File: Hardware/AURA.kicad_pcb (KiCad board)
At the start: 2 copper layers, 126.9 x 80.6 mm, 13 parts, among them SW1 EC11E18244AU, SW2 SW_Push, SW3 SW_Push, SW4 SW_Push, SW5 SW_Push, SW6 SW_Push, SW7 SW_Push, U1 ER_OLEDM0.91_1x-I2C

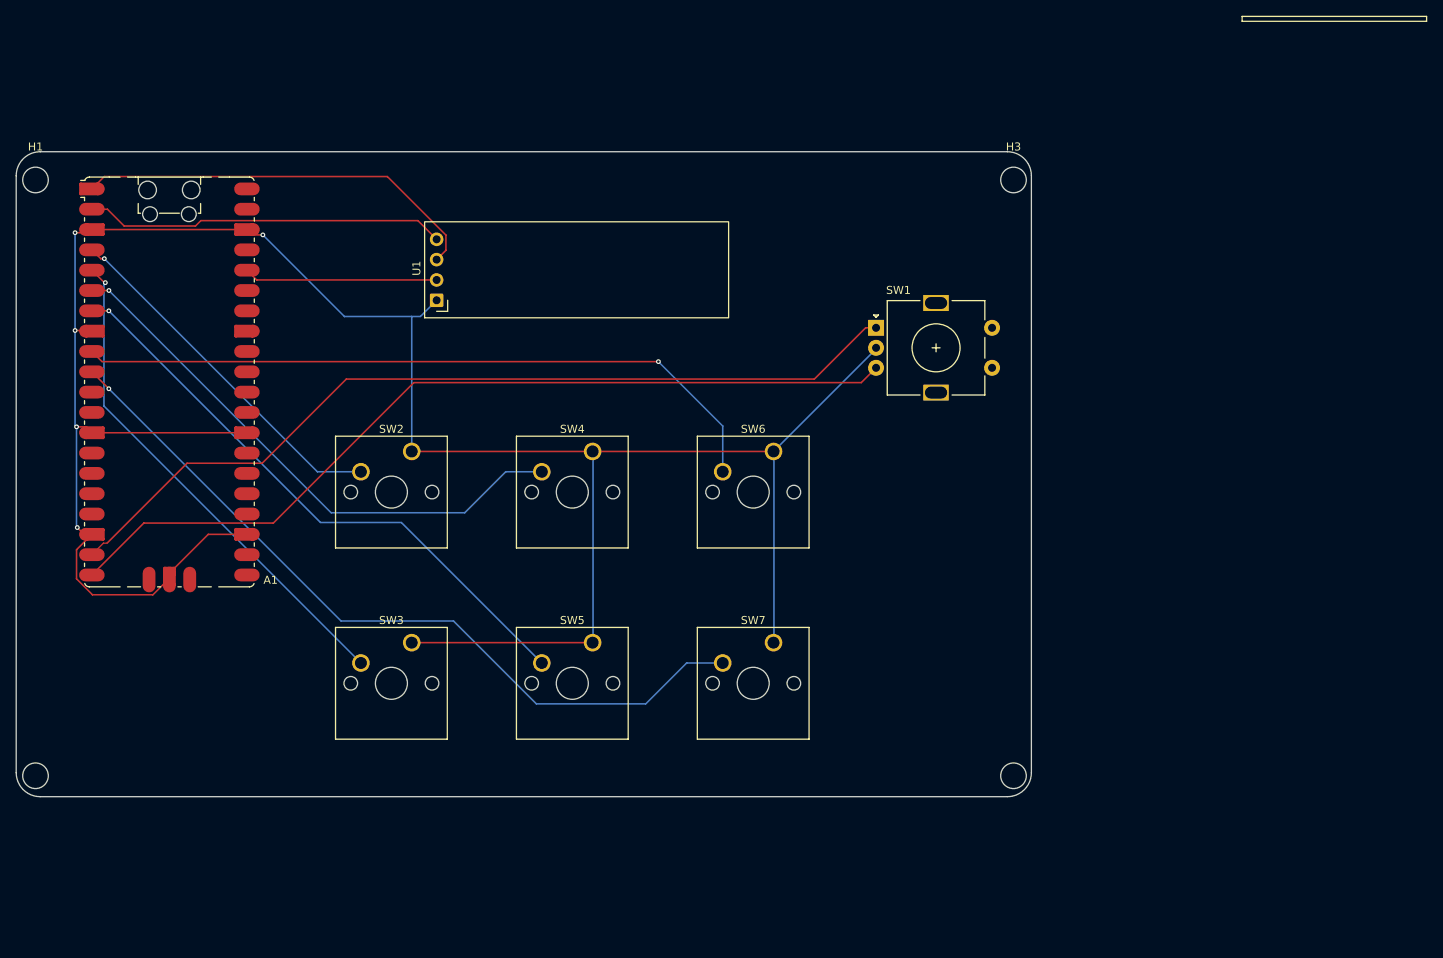
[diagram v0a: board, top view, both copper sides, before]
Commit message: AURA V2
Re-wrote the full readme. added the new .step file of the PCB, and added all the required file for the enclosure.
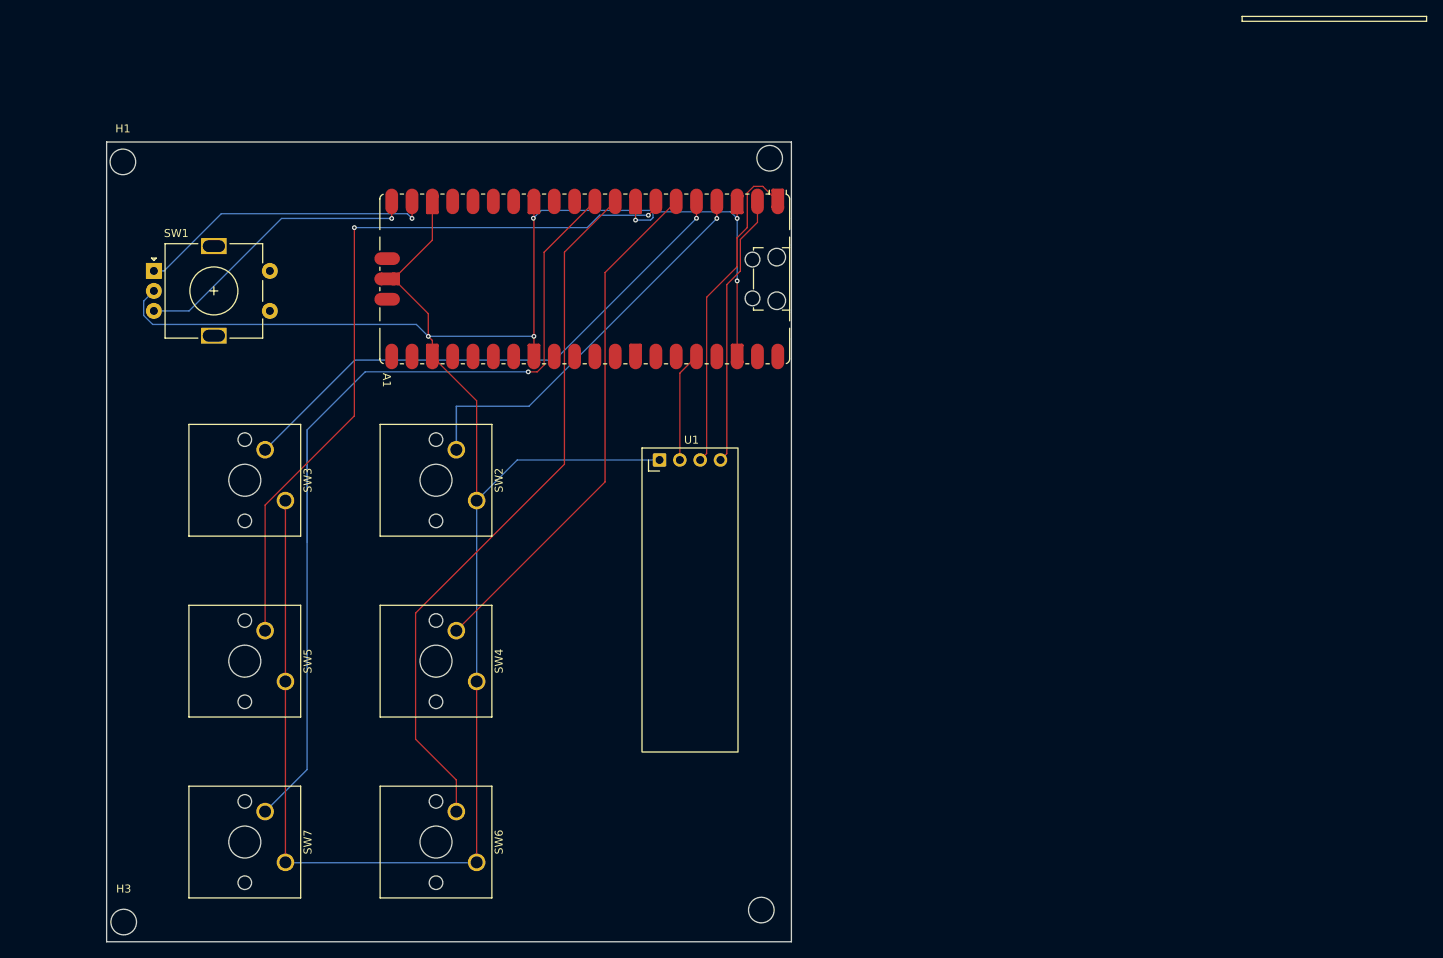
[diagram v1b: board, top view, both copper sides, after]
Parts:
- moved H3 144.8 mm to (79.2, 166.2)
- moved H2 119.9 mm to (160.0, 70.7)
- moved SW1 90.6 mm to (83.0, 84.8)
- moved SW7 66.9 mm to (99.5, 158.7), turned to -90 degrees
- moved SW6 63.4 mm to (123.4, 158.7), turned to -90 degrees
- moved A1 53.5 mm to (136.9, 85.8), turned to -90 degrees
- moved SW5 38.7 mm to (99.5, 136.1), turned to -90 degrees
- moved H4 35.7 mm to (159.0, 164.7)
- moved U1 34.3 mm to (146.2, 108.4), turned to 0 degrees
- moved SW4 32.2 mm to (123.4, 136.1), turned to -90 degrees
- moved SW3 23.8 mm to (99.5, 113.5), turned to -90 degrees
- moved H1 11.2 mm to (79.1, 71.2)
- moved SW2 10.2 mm to (123.4, 113.5), turned to -90 degrees
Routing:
- net Net-(A1-GPIO14): track 109.8 -> 37.6 mm, vias 0 -> 1
- net Net-(A1-GPIO15): track 108.7 -> 36.6 mm, vias 0 -> 1
- net Net-(A1-GPIO5): track 74.5 -> 94.5 mm, vias 1 -> 2
- net Net-(A1-GPIO1): track 45.2 -> 34.2 mm
- net GND: track 296.4 -> 307.2 mm, vias 5 -> 6
- net Net-(A1-GPIO0): track 51.5 -> 40.8 mm
- net +3.3V: track 24.2 -> 13.8 mm
- net Net-(A1-GPIO7): track 98.2 -> 105.9 mm
- net Net-(A1-GPIO4): track 69.9 -> 65.0 mm, vias 1 -> 0
- net Net-(A1-GPIO3): track 63.2 -> 68.0 mm
- net Net-(A1-GPIO2): track 45.1 -> 49.9 mm
- net Net-(A1-GPIO6): track 88.4 -> 88.7 mm, vias 1 -> 0
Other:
- board size 126.9 x 80.6 mm -> 85.6 x 100 mm
